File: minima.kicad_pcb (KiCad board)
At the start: 2 copper layers, 200.7 x 99.1 mm, 154 parts, among them J101 left_output, J102 left_input, J103 right_output, J104 right_input, J105 aux_power, J106 mains_voltage, J107 transformer_secondary, J108 transformer_primary, J109 earth, U201 LM1875, U202 LM1875, U301 NE5532, U302 NE5532, U303 NE5532, U304 NE5532, U401 LM7815_TO220, U402 LM7915_TO220

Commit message: The board shall now support single channel only.
Signed-off-by: Nenad Radulovic <nenad.radulovic@seavus.com>
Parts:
- removed C211, C218, C322, C324, C326, C328, C330, C332: 100n, Capacitor_SMD:C_1206_3216Metric_Pad1.24x1.80mm_HandSolder
- removed C212: 100u, Capacitor_THT:CP_Radial_D8.0mm_P3.50mm
- removed C213, C216, C219: 470u, Capacitor_THT:CP_Radial_D10.0mm_P5.00mm
- removed C214, C215, C220: 15p, Capacitor_SMD:C_0805_2012Metric_Pad1.15x1.50mm_HandSolder
- removed C217: 220n, Capacitor_SMD:C_1206_3216Metric_Pad1.24x1.80mm_HandSolder
- removed C321, C323, C325, C327, C329, C331: 10u, Capacitor_THT:CP_Radial_D5.0mm_P2.00mm
- removed C406, C408: 470n, Capacitor_THT:C_Rect_L9.0mm_W3.6mm_P7.50mm_MKT
- removed C407: 10n, Capacitor_THT:C_Rect_L9.0mm_W3.4mm_P7.50mm_MKT
- removed C409, C410: 10m, Capacitor_THT:CP_Radial_D35.0mm_P10.00mm_SnapIn
- removed D204: 1N5404, Diode_THT:D_DO-201AD_P12.70mm_Horizontal
- removed D303, D304: BAT54S, Package_TO_SOT_SMD:SOT-23_Handsoldering
- removed D401, D402: 1N4007, Diode_THT:D_DO-41_SOD81_P10.16mm_Horizontal
- removed D403: GBU1510, Diode_THT:Diode_Bridge_Vishay_GBU
- removed J105: aux_power, Connector_Phoenix_MC:PhoenixContact_MCV_1,5_4-G-3.5_1x04_P3.50mm_Vertical
- removed J106: mains_voltage, Connector_Phoenix_MC:PhoenixContact_MCV_1,5_2-G-3.81_1x02_P3.81mm_Vertical
- removed J107: transformer_secondary, Connector_Phoenix_MC:PhoenixContact_MCV_1,5_3-G-3.5_1x03_P3.50mm_Vertical
- removed J108: transformer_primary, Connector_Phoenix_MC:PhoenixContact_MCV_1,5_2-G-3.81_1x02_P3.81mm_Vertical
- removed J109: earth, Connector_Phoenix_MC:PhoenixContact_MCV_1,5_2-G-5.08_1x02_P5.08mm_Vertical
- removed L202: 2u, Choke_Axial_ThroughHole:Choke_Horizontal_RM15mm
- removed MH1, MH2: Mounting hole, MountingHole:MountingHole_3.2mm_M3_ISO14580_Pad
- removed MH3, MH4: Mounting Hole, MountingHole:MountingHole_3.2mm_M3_ISO14580_Pad
- removed R212, R219, R220, R224, R225: 3k9, Resistor_SMD:R_1206_3216Metric
- removed R213, R214, R226: 1k6, Resistor_SMD:R_1206_3216Metric
- removed R215, R221: 4.7, Resistor_THT:R_Axial_DIN0411_L9.9mm_D3.6mm_P15.24mm_Horizontal
- removed R216: 10, Resistor_THT:R_Axial_DIN0411_L9.9mm_D3.6mm_P15.24mm_Horizontal
- removed R217, R218, R222, R223: 270, Resistor_SMD:R_1206_3216Metric
- removed R321, R322, R323, R324: 100, Resistor_SMD:R_1206_3216Metric
- removed R405: 1, Resistor_THT:R_Axial_DIN0309_L9.0mm_D3.2mm_P12.70mm_Horizontal
- removed R406: 5k1, Resistor_THT:R_Axial_DIN0411_L9.9mm_D3.6mm_P12.70mm_Horizontal
- removed U202: LM1875, TO_SOT_Packages_THT:TO-220-5_Pentawatt_Multiwatt-5_Vertical_StaggeredType1
- removed U303, U304: NE5532, Housings_DIP:DIP-8_W7.62mm_LongPads
- removed U401: LM7815_TO220, TO_SOT_Packages_THT:TO-220_Vertical
- removed U402: LM7915_TO220, TO_SOT_Packages_THT:TO-220_Vertical
- added K201: FINDER-40.51, Relays_THT:Relay_SPDT_Finder_40.51, F.Cu at (182.6, 98.7)
- added LOGO1: KiCad Logo, Symbol:KiCad-Logo2_12mm_SilkScreen, F.Cu at (58.6, 118.7)
- added LOGO2: OSHW Logo, Symbol:OSHW-Logo2_14.6x12mm_SilkScreen, F.Cu at (210.6, 94.7)
- added MK101: Mounting_Hole, MountingHole:MountingHole_3.2mm_M3_ISO7380, F.Cu at (101.6, 51.7)
- added MK102: Mounting_Hole, MountingHole:MountingHole_3.2mm_M3_ISO7380, F.Cu at (101.6, 139.7)
- added MK103: Mounting_Hole, MountingHole:MountingHole_3.2mm_M3_ISO7380, F.Cu at (189.6, 139.7)
- added MK104: Mounting_Hole, MountingHole:MountingHole_3.2mm_M3_ISO7380, F.Cu at (189.6, 51.7)
- added Q401: PN2222A, Package_TO_SOT_THT:TO-92_Inline_Narrow_Oval, F.Cu at (187.6, 107.7)
- C202: value 100n -> 470u; footprint Capacitor_SMD:C_1206_3216Metric_Pad1.24x1.80mm_HandSolder -> Capacitor_THT:CP_Radial_D8.0mm_P3.50mm; moved to F.Cu
- C203: value 100u -> 220n; footprint Capacitor_THT:CP_Radial_D8.0mm_P3.50mm -> Capacitor_SMD:C_1206_3216Metric_Pad1.24x1.80mm_HandSolder; moved to B.Cu
- C204: moved to F.Cu
- C205: value 100u -> 100n; footprint Capacitor_THT:CP_Radial_D8.0mm_P3.50mm -> Capacitor_SMD:C_1206_3216Metric_Pad1.24x1.80mm_HandSolder
- C206: value 470u -> 100u; footprint Capacitor_THT:CP_Radial_D10.0mm_P5.00mm -> Capacitor_THT:CP_Radial_D8.0mm_P3.50mm
- C207: value 220n -> 470u; footprint Capacitor_SMD:C_1206_3216Metric_Pad1.24x1.80mm_HandSolder -> Capacitor_THT:CP_Radial_D8.0mm_P3.50mm; moved to F.Cu
- C209: value 100n -> 100u; footprint Capacitor_SMD:C_1206_3216Metric_Pad1.24x1.80mm_HandSolder -> Capacitor_THT:CP_Radial_D8.0mm_P3.50mm; moved to F.Cu
- C210: value 100u -> 15p; footprint Capacitor_THT:CP_Radial_D8.0mm_P3.50mm -> Capacitor_SMD:C_0805_2012Metric_Pad1.15x1.50mm_HandSolder; moved to B.Cu
- C301: value 10u -> 22p; footprint Capacitor_THT:CP_Radial_D5.0mm_P2.00mm -> Capacitor_SMD:C_0805_2012Metric_Pad1.15x1.50mm_HandSolder
- C302, C315, C317: value 10u -> 22u
- C303: value 10u -> 220p; footprint Capacitor_THT:CP_Radial_D5.0mm_P2.00mm -> Capacitor_SMD:C_0805_2012Metric_Pad1.15x1.50mm_HandSolder; moved to B.Cu
- C304: value 10u -> 1n; footprint Capacitor_THT:CP_Radial_D5.0mm_P2.00mm -> Capacitor_SMD:C_0805_2012Metric_Pad1.15x1.50mm_HandSolder; moved to B.Cu
- C305: value 220p -> 22p
- C306: value 1n -> 22p
- C307, C308, D301, D302: moved to B.Cu
- C309: value 220p -> 22u; footprint Capacitor_SMD:C_0805_2012Metric_Pad1.15x1.50mm_HandSolder -> Capacitor_THT:CP_Radial_D5.0mm_P2.00mm
- C310, C312: value 1n -> 22u; footprint Capacitor_SMD:C_0805_2012Metric_Pad1.15x1.50mm_HandSolder -> Capacitor_THT:CP_Radial_D5.0mm_P2.00mm
- C311: value 220p -> 100n; footprint Capacitor_SMD:C_0805_2012Metric_Pad1.15x1.50mm_HandSolder -> Capacitor_SMD:C_1206_3216Metric_Pad1.24x1.80mm_HandSolder
- C313, C314, C316, C319: value 10u -> 100n; footprint Capacitor_THT:CP_Radial_D5.0mm_P2.00mm -> Capacitor_SMD:C_1206_3216Metric_Pad1.24x1.80mm_HandSolder
- C320: value 100n -> 22p; footprint Capacitor_SMD:C_1206_3216Metric_Pad1.24x1.80mm_HandSolder -> Capacitor_SMD:C_0805_2012Metric_Pad1.15x1.50mm_HandSolder
- C401, C403: value 1m -> 4m7; footprint Capacitor_THT:CP_Radial_D12.5mm_P5.00mm -> Capacitor_THT:CP_Radial_D25.0mm_P10.00mm_SnapIn
- C402, C404: value 10u -> 1m; footprint Capacitor_THT:CP_Radial_D5.0mm_P2.00mm -> Capacitor_THT:CP_Radial_D12.5mm_P5.00mm
- C405: value 10n -> 100n; footprint Capacitor_THT:C_Rect_L13.0mm_W4.0mm_P10.00mm_FKS3_FKP3_MKS4 -> Capacitor_SMD:C_1206_3216Metric_Pad1.24x1.80mm_HandSolder
- D203: value 1N5404 -> 1N4148; footprint Diode_THT:D_DO-201AD_P12.70mm_Horizontal -> Diodes_THT:D_DO-35_SOD27_P7.62mm_Horizontal
- J101: value left_output -> output
- J102: value left_input -> input; footprint Connector_PinHeader_2.54mm:PinHeader_1x04_P2.54mm_Vertical -> TerminalBlock_Phoenix:TerminalBlock_Phoenix_MPT-0,5-4-2.54_1x04_P2.54mm_Horizontal
- J103: value right_output -> powersupply; footprint Connector_Phoenix_MC:PhoenixContact_MCV_1,5_2-G-3.5_1x02_P3.50mm_Vertical -> Connector_Phoenix_MC:PhoenixContact_MCV_1,5_6-G-3.5_1x06_P3.50mm_Vertical
- J104: value right_input -> ps_ctrl; footprint Connector_PinHeader_2.54mm:PinHeader_1x04_P2.54mm_Vertical -> Connector_IDC:IDC-Header_2x05_P2.54mm_Vertical
- R201: footprint Resistor_SMD:R_1206_3216Metric -> Resistor_SMD:R_1206_3216Metric_Pad1.24x1.80mm_HandSolder
- R202: value 4.7 -> 15k; footprint Resistor_THT:R_Axial_DIN0411_L9.9mm_D3.6mm_P15.24mm_Horizontal -> Resistor_SMD:R_1206_3216Metric_Pad1.24x1.80mm_HandSolder; moved to B.Cu
- R203: value 10 -> 4.7
- R204: value 270 -> 10; footprint Resistor_SMD:R_1206_3216Metric -> Resistor_THT:R_Axial_DIN0411_L9.9mm_D3.6mm_P15.24mm_Horizontal; moved to F.Cu
- R205: value 270 -> 499; footprint Resistor_SMD:R_1206_3216Metric -> Resistor_SMD:R_1206_3216Metric_Pad1.24x1.80mm_HandSolder
- R206: value 3k9 -> 15k; footprint Resistor_SMD:R_1206_3216Metric -> Resistor_SMD:R_1206_3216Metric_Pad1.24x1.80mm_HandSolder
- R207: value 3k9 -> 4.7; footprint Resistor_SMD:R_1206_3216Metric -> Resistor_THT:R_Axial_DIN0411_L9.9mm_D3.6mm_P15.24mm_Horizontal; moved to F.Cu
- R208: value 4.7 -> 499; footprint Resistor_THT:R_Axial_DIN0411_L9.9mm_D3.6mm_P15.24mm_Horizontal -> Resistor_SMD:R_1206_3216Metric_Pad1.24x1.80mm_HandSolder; moved to B.Cu
- R209, R210: value 270 -> 15k; footprint Resistor_SMD:R_1206_3216Metric -> Resistor_SMD:R_1206_3216Metric_Pad1.24x1.80mm_HandSolder
- R211: value 3k9 -> 1k6; footprint Resistor_SMD:R_1206_3216Metric -> Resistor_SMD:R_1206_3216Metric_Pad1.24x1.80mm_HandSolder
- R301, R304, R317, R318: value 10 -> 2k; footprint Resistor_SMD:R_1206_3216Metric -> Resistor_SMD:R_1206_3216Metric_Pad1.24x1.80mm_HandSolder
- R302, R303: value 10 -> 100; footprint Resistor_SMD:R_1206_3216Metric -> Resistor_SMD:R_1206_3216Metric_Pad1.24x1.80mm_HandSolder; moved to B.Cu
- R305: value 100 -> 49.9; footprint Resistor_SMD:R_1206_3216Metric -> Resistor_SMD:R_1206_3216Metric_Pad1.24x1.80mm_HandSolder
- R306: value 100 -> 2k; footprint Resistor_SMD:R_1206_3216Metric -> Resistor_SMD:R_1206_3216Metric_Pad1.24x1.80mm_HandSolder
- R307: value 100 -> 100k; footprint Resistor_SMD:R_1206_3216Metric -> Resistor_SMD:R_1206_3216Metric_Pad1.24x1.80mm_HandSolder; moved to B.Cu
- R308: value 100 -> 11k; footprint Resistor_SMD:R_1206_3216Metric -> Resistor_SMD:R_1206_3216Metric_Pad1.24x1.80mm_HandSolder; moved to B.Cu
- R309, R313: value 100k -> 2k; footprint Resistor_SMD:R_1206_3216Metric -> Resistor_SMD:R_1206_3216Metric_Pad1.24x1.80mm_HandSolder
- R310: value 10k -> 2k; footprint Resistor_SMD:R_1206_3216Metric -> Resistor_SMD:R_1206_3216Metric_Pad1.24x1.80mm_HandSolder
- R311: footprint Resistor_SMD:R_1206_3216Metric -> Resistor_SMD:R_1206_3216Metric_Pad1.24x1.80mm_HandSolder; moved to B.Cu
- R312: value 10k -> 11k; footprint Resistor_SMD:R_1206_3216Metric -> Resistor_SMD:R_1206_3216Metric_Pad1.24x1.80mm_HandSolder; moved to B.Cu
- R314: value 10k -> 49.9; footprint Resistor_SMD:R_1206_3216Metric -> Resistor_SMD:R_1206_3216Metric_Pad1.24x1.80mm_HandSolder
- R315: value 100k -> 100; footprint Resistor_SMD:R_1206_3216Metric -> Resistor_SMD:R_1206_3216Metric_Pad1.24x1.80mm_HandSolder; moved to B.Cu
- R316: value 10k -> 100; footprint Resistor_SMD:R_1206_3216Metric -> Resistor_SMD:R_1206_3216Metric_Pad1.24x1.80mm_HandSolder; moved to B.Cu
- R319, R320: value 10 -> 49.9; footprint Resistor_SMD:R_1206_3216Metric -> Resistor_SMD:R_1206_3216Metric_Pad1.24x1.80mm_HandSolder
- R401, R402: value 47 -> 1
- R403: value 1 -> 10; footprint Resistor_THT:R_Axial_DIN0309_L9.0mm_D3.2mm_P12.70mm_Horizontal -> Resistor_THT:R_Axial_DIN0411_L9.9mm_D3.6mm_P12.70mm_Horizontal
- R404: value 5k1 -> 1k; footprint Resistor_THT:R_Axial_DIN0411_L9.9mm_D3.6mm_P12.70mm_Horizontal -> Resistor_SMD:R_1206_3216Metric_Pad1.24x1.80mm_HandSolder; moved to B.Cu
- moved R303 378.1 mm to (109.6, 128.7)
- moved C309 378.1 mm to (117.6, 121.7), turned to 270 degrees
- moved R304 372.4 mm to (100.6, 88.2)
- moved R308 367.8 mm to (109.6, 119.2)
- moved C310 367.7 mm to (116.6, 78.7)
- moved R316 365.2 mm to (117.6, 128.7), turned to 180 degrees
- moved R312 364.6 mm to (117.6, 119.2)
- moved R302 363.5 mm to (108.1, 132.7), turned to 270 degrees
- moved R306 362.1 mm to (100.6, 92.7)
- moved R307 361.5 mm to (109.6, 126.2)
- moved C312 357.4 mm to (115.6, 60.7), turned to 180 degrees
- moved D302 356.5 mm to (123.1, 132.7), turned to 180 degrees
- moved C302 354.4 mm to (109.6, 121.7), turned to 270 degrees
- moved C308 351.9 mm to (115.6, 131.7)
- moved C315 348.2 mm to (110.6, 96.7), turned to 180 degrees
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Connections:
- C201 pad 1: Net-(C201-Pad1) -> /Input section/sgnd
- C202 pad 1: VCC -> Net-(C202-Pad1)
- C202 pad 2: GNDPWR -> /Power amplifier/inp
- C203 pad 1: VCC -> Net-(C203-Pad1)
- C203 pad 2: GNDPWR -> Net-(C203-Pad2)
- C204 pad 1: VCC -> Net-(C204-Pad1)
- C204 pad 2: GNDPWR -> /Power amplifier/spkhot
- C206 pad 1: Net-(C206-Pad1) -> VCC
- C206 pad 2: /Power amplifier/left_inp -> GNDPWR
- C207 pad 2: Net-(C207-Pad2) -> /Power amplifier/inn
- C208 pad 1: Net-(C208-Pad1) -> GNDPWR
- C208 pad 2: /Power amplifier/left_spkhot -> VEE
- C210 pad 1: GNDPWR -> Net-(C203-Pad2)
- C210 pad 2: VEE -> Net-(C210-Pad2)
- C301 pad 2: Net-(C301-Pad2) -> /Input section/sgnd
- C303 pad 1: Net-(C301-Pad1) -> Net-(C303-Pad1)
- C303 pad 2: Net-(C301-Pad2) -> /Input section/sgnd
- C304 pad 1: Net-(C302-Pad1) -> Net-(C302-Pad2)
- C304 pad 2: Net-(C302-Pad2) -> /Input section/sgnd
- C305 pad 2: GNDPWR -> Net-(C305-Pad2)
- C306 pad 1: Net-(C301-Pad2) -> Net-(C306-Pad1)
- C306 pad 2: GNDPWR -> /Input section/sgnd
- C307 pad 1: Net-(C307-Pad1) -> /Input section/sgnd
- C307 pad 2: GNDPWR -> Net-(C307-Pad2)
- C308 pad 1: Net-(C302-Pad2) -> /Input section/sgnd
- C308 pad 2: GNDPWR -> Net-(C308-Pad2)
- C309 pad 1: GNDPWR -> Net-(C309-Pad1)
- C309 pad 2: Net-(C309-Pad2) -> Net-(C308-Pad2)
- C310 pad 1: GNDPWR -> VDDA
- C310 pad 2: Net-(C310-Pad2) -> GNDPWR
- C311 pad 1: GNDPWR -> VDDA
- C311 pad 2: Net-(C311-Pad2) -> GNDPWR
- C312 pad 1: GNDPWR -> VDDA
- C312 pad 2: Net-(C312-Pad2) -> GNDPWR
- C313 pad 1: Net-(C313-Pad1) -> VDDA
- C313 pad 2: Net-(C310-Pad2) -> GNDPWR
- C314 pad 1: Net-(C314-Pad1) -> VDDA
- C314 pad 2: Net-(C312-Pad2) -> GNDPWR
- C315 pad 1: Net-(C313-Pad1) -> GNDPWR
- C315 pad 2: Net-(C310-Pad2) -> VSSA
- C316 pad 1: Net-(C314-Pad1) -> GNDPWR
- C316 pad 2: Net-(C312-Pad2) -> VSSA
- C317 pad 1: VDDA -> GNDPWR
- C317 pad 2: GNDPWR -> VSSA
- C318 pad 1: VDDA -> GNDPWR
- C318 pad 2: GNDPWR -> VSSA
- C319 pad 1: VDDA -> GNDPWR
- C319 pad 2: GNDPWR -> VSSA
- C320 pad 1: VDDA -> Net-(C320-Pad1)
- C320 pad 2: GNDPWR -> Net-(C320-Pad2)
- C401 pad 1: Net-(C401-Pad1) -> VCC
- C403 pad 2: Net-(C403-Pad2) -> VEE
- C405 pad 1: /Power supply/m2 -> GNDPWR
- C405 pad 2: /Power supply/m1 -> /Input section/sgnd
- D201 pad 2: /Power amplifier/left_spkhot -> /Power amplifier/spkhot
- D202 pad 1: /Power amplifier/left_spkhot -> /Power amplifier/spkhot
- D203 pad 1: VCC -> /Power amplifier/mutep
- D203 pad 2: /Power amplifier/right_spkhot -> /Power amplifier/muten
- D301 pad 3: Net-(C305-Pad1) -> Net-(C303-Pad1)
- D302 pad 3: Net-(C307-Pad1) -> Net-(C307-Pad2)
- J101 pad 1: /Power amplifier/left_spkhot -> /Power amplifier/spkhot
- J102 pad 1: /Input section/left_inp -> /Input section/inp
- J102 pad 2: GNDPWR -> /Input section/sgnd
- J102 pad 3: /Input section/left_inn -> /Input section/inn
- J102 pad 4: GNDPWR -> /Input section/sgnd
- J103 pad 1: /Power amplifier/right_spkhot -> /Power supply/ps_prevcc
- J103 pad 2: GNDPWR -> /Power supply/ps_prevee
- J104 pad 1: /Input section/right_inp -> /Power amplifier/mutep
- J104 pad 2: GNDPWR -> /Power supply/ps_ctrl_gnd
- J104 pad 3: /Input section/right_inn -> /Power supply/ps_ctrl_gnd
- J104 pad 4: GNDPWR -> /Power supply/ps_ctrl_op
- L201 pad 1: Net-(C207-Pad2) -> Net-(C203-Pad2)
- L201 pad 2: /Power amplifier/left_spkhot -> /Power amplifier/outp
- R201 pad 1: Net-(C201-Pad1) -> Net-(R201-Pad1)
- R201 pad 2: GNDPWR -> Net-(C201-Pad2)
- R202 pad 1: GNDPWR -> /Input section/sgnd
- R202 pad 2: Net-(C207-Pad1) -> Net-(R201-Pad1)
- R203 pad 2: Net-(C208-Pad1) -> Net-(C203-Pad1)
- R204 pad 1: Net-(R204-Pad1) -> GNDPWR
- R204 pad 2: Net-(C206-Pad1) -> Net-(C204-Pad1)
- R205 pad 1: Net-(C201-Pad2) -> Net-(R201-Pad1)
- R205 pad 2: Net-(R204-Pad1) -> Net-(C202-Pad1)
- R206 pad 1: Net-(R206-Pad1) -> /Input section/sgnd
- R206 pad 2: Net-(C201-Pad2) -> Net-(R201-Pad1)
- R207 pad 1: GNDPWR -> /Power amplifier/outp
- R207 pad 2: Net-(R206-Pad1) -> Net-(C203-Pad2)
- R208 pad 1: /Power amplifier/left_spkhot -> Net-(R208-Pad1)
- R208 pad 2: Net-(C207-Pad2) -> Net-(C207-Pad1)
- R209 pad 1: Net-(R209-Pad1) -> Net-(C203-Pad2)
- R209 pad 2: Net-(C213-Pad1) -> Net-(R208-Pad1)
- R210 pad 1: Net-(C214-Pad2) -> Net-(C203-Pad2)
- R210 pad 2: Net-(R209-Pad1) -> Net-(R208-Pad1)
- R211 pad 1: Net-(R211-Pad1) -> Net-(R208-Pad1)
- R211 pad 2: Net-(C214-Pad2) -> Net-(C210-Pad2)
- R301 pad 1: /Power amplifier/left_inp -> /Input section/sgnd
- R301 pad 2: Net-(R301-Pad2) -> Net-(C301-Pad1)
- R302 pad 1: /Power amplifier/left_inp -> Net-(C303-Pad1)
- R302 pad 2: Net-(R302-Pad2) -> /Input section/inp
- R303 pad 1: /Power amplifier/right_inp -> Net-(C302-Pad2)
- R303 pad 2: Net-(R303-Pad2) -> Net-(C303-Pad1)
- R304 pad 1: /Power amplifier/right_inp -> Net-(C301-Pad1)
- R305 pad 1: Net-(C305-Pad1) -> /Power amplifier/inp
- R305 pad 2: /Input section/left_inp -> Net-(C305-Pad2)
- R306 pad 1: Net-(C301-Pad2) -> Net-(C305-Pad1)
- R306 pad 2: Net-(C305-Pad1) -> Net-(R306-Pad2)
- R307 pad 1: Net-(C307-Pad1) -> Net-(C302-Pad2)
- R307 pad 2: /Input section/right_inp -> /Input section/sgnd
- R308 pad 1: Net-(C302-Pad2) -> Net-(C302-Pad1)
- R308 pad 2: Net-(C307-Pad1) -> /Input section/sgnd
- R309 pad 1: Net-(C301-Pad2) -> Net-(C305-Pad2)
- R309 pad 2: GNDPWR -> Net-(C305-Pad1)
- R310 pad 1: Net-(C301-Pad1) -> /Input section/sgnd
- R310 pad 2: GNDPWR -> Net-(C306-Pad1)
- R311 pad 1: Net-(C302-Pad2) -> /Input section/sgnd
- R311 pad 2: GNDPWR -> Net-(C308-Pad2)
- R312 pad 1: Net-(C302-Pad1) -> /Input section/sgnd
- R312 pad 2: GNDPWR -> Net-(C309-Pad1)
- R313 pad 1: GNDPWR -> Net-(C306-Pad1)
- R313 pad 2: Net-(C310-Pad2) -> Net-(R304-Pad2)
- R314 pad 1: GNDPWR -> /Power amplifier/inp
- R314 pad 2: Net-(C313-Pad1) -> Net-(C320-Pad2)
- R315 pad 1: GNDPWR -> Net-(C307-Pad2)
- R315 pad 2: Net-(C312-Pad2) -> /Input section/inn
- R316 pad 1: GNDPWR -> Net-(C308-Pad2)
- R316 pad 2: Net-(C314-Pad1) -> Net-(C307-Pad2)
- R317 pad 1: /Power amplifier/left_inn -> Net-(C320-Pad1)
- R317 pad 2: Net-(R317-Pad2) -> Net-(R306-Pad2)
- R318 pad 1: /Power amplifier/left_inn -> Net-(C320-Pad2)
- R318 pad 2: Net-(R318-Pad2) -> Net-(C320-Pad1)
- R319 pad 1: /Power amplifier/right_inn -> /Power amplifier/inn
- R319 pad 2: Net-(R319-Pad2) -> /Input section/sgnd
- R320 pad 1: /Power amplifier/right_inn -> /Power amplifier/inn
- R320 pad 2: Net-(R320-Pad2) -> /Input section/sgnd
- R401 pad 1: Net-(C401-Pad1) -> VDDA
- R401 pad 2: VCC -> /Power supply/ps_prevcc
- R402 pad 1: Net-(C403-Pad2) -> VSSA
- R402 pad 2: VEE -> /Power supply/ps_prevee
- R403 pad 1: Net-(C406-Pad2) -> /Input section/sgnd
- R404 pad 1: VCC -> Net-(Q401-Pad2)
- R404 pad 2: GNDPWR -> /Power supply/ps_ctrl_op
- U201 pad 1: Net-(C201-Pad2) -> Net-(R201-Pad1)
- U201 pad 2: Net-(C214-Pad2) -> Net-(R208-Pad1)
- U201 pad 4: Net-(C207-Pad2) -> Net-(C203-Pad2)
- U301 pad 1: Net-(R301-Pad2) -> Net-(R304-Pad2)
- U301 pad 2: Net-(R301-Pad2) -> Net-(R304-Pad2)
- U301 pad 3: Net-(C301-Pad1) -> Net-(C302-Pad1)
- U301 pad 5: Net-(C301-Pad1) -> Net-(C309-Pad1)
- U301 pad 6: Net-(R302-Pad2) -> Net-(R306-Pad2)
- U301 pad 7: Net-(R302-Pad2) -> Net-(R306-Pad2)
- U302 pad 1: Net-(R303-Pad2) -> Net-(C305-Pad2)
- U302 pad 2: Net-(R303-Pad2) -> Net-(C305-Pad1)
- U302 pad 3: Net-(C302-Pad1) -> Net-(C301-Pad1)
- U302 pad 5: Net-(C302-Pad1) -> Net-(C306-Pad1)
- U302 pad 6: Net-(R304-Pad2) -> Net-(C320-Pad1)
- U302 pad 7: Net-(R304-Pad2) -> Net-(C320-Pad2)
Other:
- board size 200.7 x 99.1 mm -> 100 x 100 mm

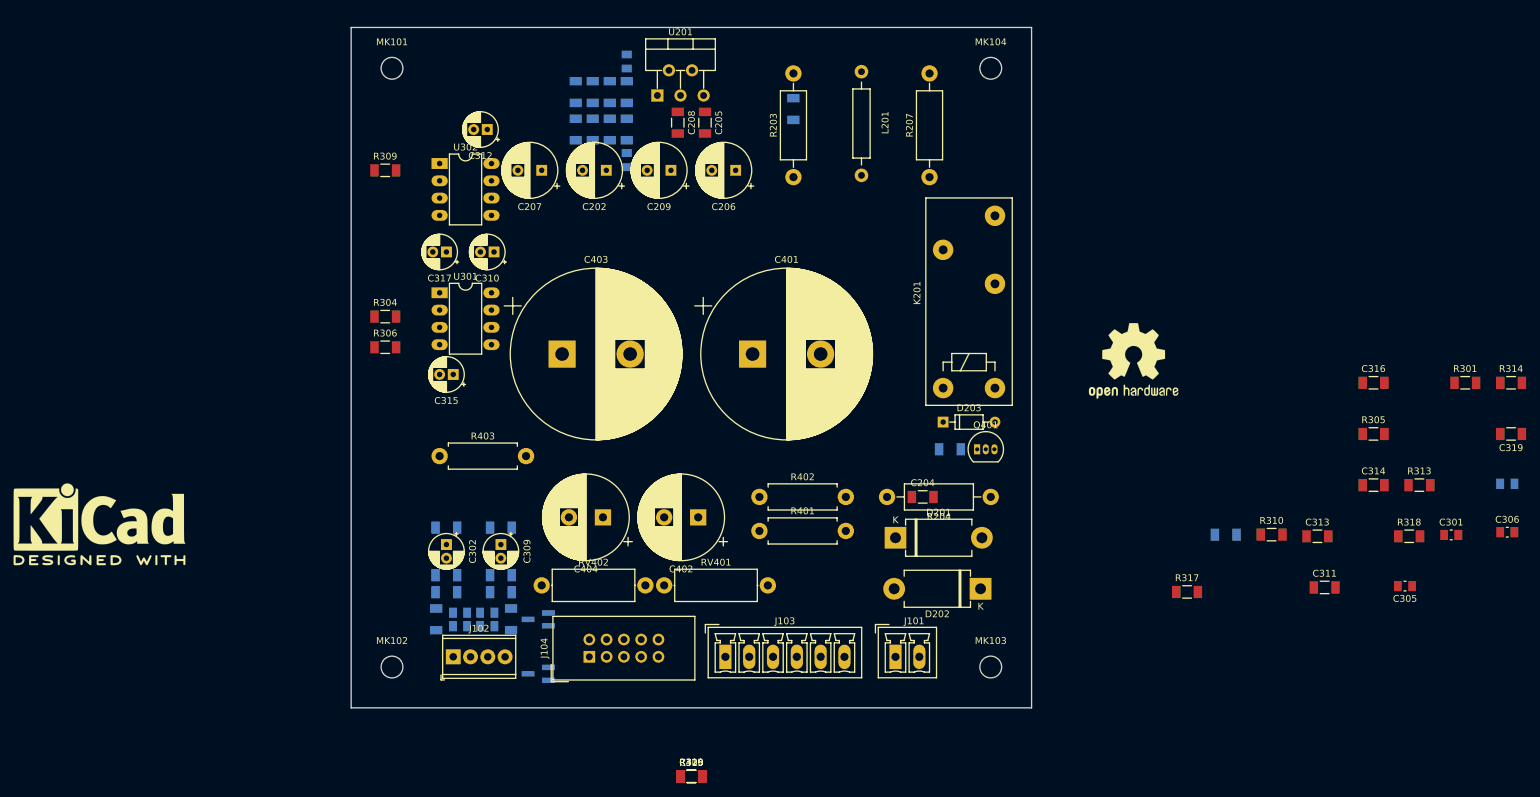
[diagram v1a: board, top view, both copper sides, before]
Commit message: Switched to Kicad 5.0
Signed-off-by: Nenad Radulovic <nenad.b.radulovic@gmail.com>
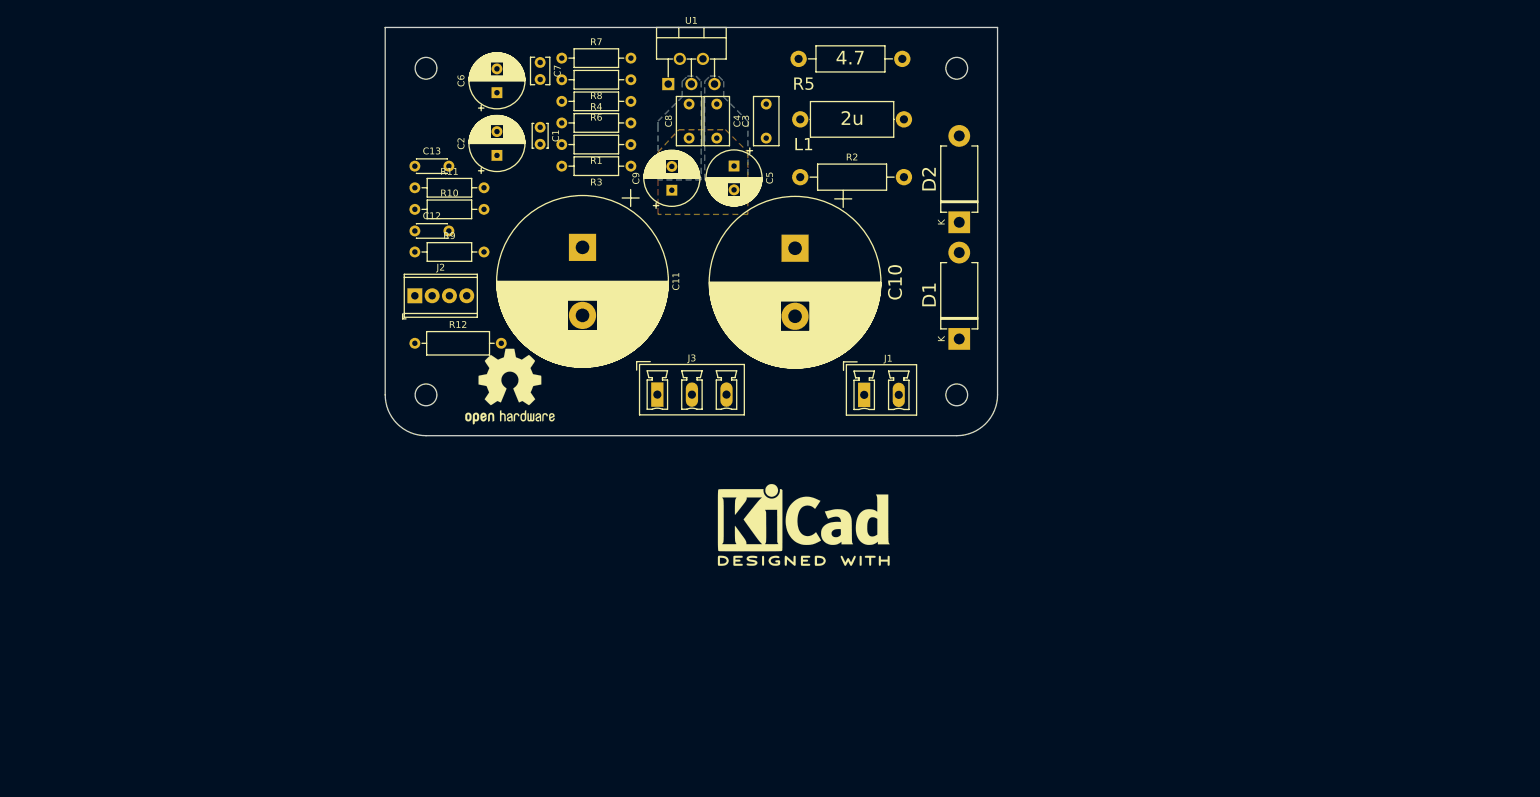
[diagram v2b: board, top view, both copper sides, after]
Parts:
- removed C201, C210: 15p, Capacitor_SMD:C_0805_2012Metric_Pad1.15x1.50mm_HandSolder
- removed C202, C207: 470u, Capacitor_THT:CP_Radial_D8.0mm_P3.50mm
- removed C203: 220n, Capacitor_SMD:C_1206_3216Metric_Pad1.24x1.80mm_HandSolder
- removed C204, C205, C208, C311, C313, C314, C316, C318, C319, C405: 100n, Capacitor_SMD:C_1206_3216Metric_Pad1.24x1.80mm_HandSolder
- removed C206, C209: 100u, Capacitor_THT:CP_Radial_D8.0mm_P3.50mm
- removed C301, C305, C306, C320: 22p, Capacitor_SMD:C_0805_2012Metric_Pad1.15x1.50mm_HandSolder
- removed C302, C309, C310, C312, C315, C317: 22u, Capacitor_THT:CP_Radial_D5.0mm_P2.00mm
- removed C303, C307: 220p, Capacitor_SMD:C_0805_2012Metric_Pad1.15x1.50mm_HandSolder
- removed C304, C308: 1n, Capacitor_SMD:C_0805_2012Metric_Pad1.15x1.50mm_HandSolder
- removed C401, C403: 4m7, Capacitor_THT:CP_Radial_D25.0mm_P10.00mm_SnapIn
- removed C402, C404: 1m, Capacitor_THT:CP_Radial_D12.5mm_P5.00mm
- removed D201, D202: 1N5404, Diode_THT:D_DO-201AD_P12.70mm_Horizontal
- removed D203: 1N4148, Diodes_THT:D_DO-35_SOD27_P7.62mm_Horizontal
- removed D301, D302: BAT54S, Package_TO_SOT_SMD:SOT-23_Handsoldering
- removed J101: output, Connector_Phoenix_MC:PhoenixContact_MCV_1,5_2-G-3.5_1x02_P3.50mm_Vertical
- removed J102: input, TerminalBlock_Phoenix:TerminalBlock_Phoenix_MPT-0,5-4-2.54_1x04_P2.54mm_Horizontal
- removed J103: powersupply, Connector_Phoenix_MC:PhoenixContact_MCV_1,5_6-G-3.5_1x06_P3.50mm_Vertical
- removed J104: ps_ctrl, Connector_IDC:IDC-Header_2x05_P2.54mm_Vertical
- removed K201: FINDER-40.51, Relays_THT:Relay_SPDT_Finder_40.51
- removed L201: 2u, Choke_Axial_ThroughHole:Choke_Horizontal_RM15mm
- removed MK101, MK102, MK103, MK104: Mounting_Hole, MountingHole:MountingHole_3.2mm_M3_ISO7380
- removed Q401: PN2222A, Package_TO_SOT_THT:TO-92_Inline_Narrow_Oval
- removed R201, R211: 1k6, Resistor_SMD:R_1206_3216Metric_Pad1.24x1.80mm_HandSolder
- removed R202, R206, R209, R210: 15k, Resistor_SMD:R_1206_3216Metric_Pad1.24x1.80mm_HandSolder
- removed R203, R207: 4.7, Resistor_THT:R_Axial_DIN0411_L9.9mm_D3.6mm_P15.24mm_Horizontal
- removed R204: 10, Resistor_THT:R_Axial_DIN0411_L9.9mm_D3.6mm_P15.24mm_Horizontal
- removed R205, R208: 499, Resistor_SMD:R_1206_3216Metric_Pad1.24x1.80mm_HandSolder
- removed R301, R304, R306, R309, R310, R313, R317, R318: 2k, Resistor_SMD:R_1206_3216Metric_Pad1.24x1.80mm_HandSolder
- removed R302, R303, R315, R316: 100, Resistor_SMD:R_1206_3216Metric_Pad1.24x1.80mm_HandSolder
- removed R305, R314, R319, R320: 49.9, Resistor_SMD:R_1206_3216Metric_Pad1.24x1.80mm_HandSolder
- removed R307, R311: 100k, Resistor_SMD:R_1206_3216Metric_Pad1.24x1.80mm_HandSolder
- removed R308, R312: 11k, Resistor_SMD:R_1206_3216Metric_Pad1.24x1.80mm_HandSolder
- removed R401, R402: 1, Resistor_THT:R_Axial_DIN0411_L9.9mm_D3.6mm_P12.70mm_Horizontal
- removed R403: 10, Resistor_THT:R_Axial_DIN0411_L9.9mm_D3.6mm_P12.70mm_Horizontal
- removed R404: 1k, Resistor_SMD:R_1206_3216Metric_Pad1.24x1.80mm_HandSolder
- removed RV401, RV402: Varistor, Resistor_THT:R_Axial_DIN0414_L11.9mm_D4.5mm_P15.24mm_Horizontal
- removed U201: LM1875, TO_SOT_Packages_THT:TO-220-5_Pentawatt_Multiwatt-5_Vertical_StaggeredType1
- removed U301, U302: NE5532, Housings_DIP:DIP-8_W7.62mm_LongPads
- added C1: 15p, Capacitor_THT:C_Disc_D3.4mm_W2.1mm_P2.50mm, F.Cu at (123.3, 60.4)
- added C10: 4m7, Capacitor_THT:CP_Radial_D25.0mm_P10.00mm_SnapIn, F.Cu at (160.8, 78.2)
- added C11: 4m7, Capacitor_THT:CP_Radial_D25.0mm_P10.00mm_SnapIn, F.Cu at (129.6, 78.0)
- added C12: 220p, Capacitor_THT:C_Disc_D4.3mm_W1.9mm_P5.00mm, F.Cu at (104.9, 75.6)
- added C13: 1n, Capacitor_THT:C_Disc_D4.3mm_W1.9mm_P5.00mm, F.Cu at (104.9, 66.1)
- added C2: 470u, Capacitor_THT:CP_Radial_D8.0mm_P3.50mm, F.Cu at (117.0, 64.5)
- added C3: 220n, Capacitor_THT:C_Rect_L7.0mm_W3.5mm_P5.00mm, F.Cu at (156.6, 62.0)
- added C4: 100n, Capacitor_THT:C_Rect_L7.0mm_W3.5mm_P5.00mm, F.Cu at (149.3, 57.0)
- added C5: 100u, Capacitor_THT:CP_Radial_D8.0mm_P3.50mm, F.Cu at (151.8, 66.1)
- added C6: 470u, Capacitor_THT:CP_Radial_D8.0mm_P3.50mm, F.Cu at (117.0, 55.3)
- added C7: 15p, Capacitor_THT:C_Disc_D3.8mm_W2.6mm_P2.50mm, F.Cu at (123.3, 50.9)
- added C8: 100n, Capacitor_THT:C_Rect_L7.0mm_W3.5mm_P5.00mm, F.Cu at (145.2, 62.0)
- added C9: 100u, Capacitor_THT:CP_Radial_D8.0mm_P3.50mm, F.Cu at (142.7, 69.6)
- added D1: 1N5404, Diode_THT:D_DO-201AD_P12.70mm_Horizontal, F.Cu at (184.9, 91.5)
- added D2: 1N5404, Diode_THT:D_DO-201AD_P12.70mm_Horizontal, F.Cu at (184.9, 74.4)
- added J1: output, Connector_Phoenix_MC_HighVoltage:PhoenixContact_MCV_1,5_2-G-5.08_1x02_P5.08mm_Vertical, F.Cu at (171.0, 99.7)
- added J2: input, TerminalBlock_Phoenix:TerminalBlock_Phoenix_MPT-0,5-4-2.54_1x04_P2.54mm_Horizontal, F.Cu at (104.9, 85.2)
- added J3: powersupply, Connector_Phoenix_MC_HighVoltage:PhoenixContact_MCV_1,5_3-G-5.08_1x03_P5.08mm_Vertical, F.Cu at (140.6, 99.7)
- added L1: 2u, Inductor_THT:L_Axial_L12.0mm_D5.0mm_P15.24mm_Horizontal_Fastron_MISC, F.Cu at (161.6, 59.2)
- added MK1: Mounting_Hole, MountingHole:MountingHole_3.2mm_M3_ISO7380, F.Cu at (106.6, 99.7)
- added MK2: Mounting_Hole, MountingHole:MountingHole_3.2mm_M3_ISO7380, F.Cu at (106.6, 51.7)
- added MK3: Mounting_Hole, MountingHole:MountingHole_3.2mm_M3_ISO7380, F.Cu at (184.6, 51.7)
- added MK4: Mounting_Hole, MountingHole:MountingHole_3.2mm_M3_ISO7380, F.Cu at (184.6, 99.7)
- added R1: 1k6, Resistor_THT:R_Axial_DIN0207_L6.3mm_D2.5mm_P10.16mm_Horizontal, F.Cu at (136.7, 62.9)
- added R10: 100, Resistor_THT:R_Axial_DIN0207_L6.3mm_D2.5mm_P10.16mm_Horizontal, F.Cu at (104.9, 72.5)
- added R11: 100k, Resistor_THT:R_Axial_DIN0207_L6.3mm_D2.5mm_P10.16mm_Horizontal, F.Cu at (104.9, 69.3)
- added R12: 10, Resistor_THT:R_Axial_DIN0309_L9.0mm_D3.2mm_P12.70mm_Horizontal, F.Cu at (104.9, 92.1)
- added R2: 4.7, Resistor_THT:R_Axial_DIN0411_L9.9mm_D3.6mm_P15.24mm_Horizontal, F.Cu at (161.6, 67.7)
- added R3: 499, Resistor_THT:R_Axial_DIN0207_L6.3mm_D2.5mm_P10.16mm_Horizontal, F.Cu at (136.7, 66.1)
- added R4: 15k, Resistor_THT:R_Axial_DIN0207_L6.3mm_D2.5mm_P10.16mm_Horizontal, F.Cu at (126.5, 59.8)
- added R5: 4.7, Resistor_THT:R_Axial_DIN0411_L9.9mm_D3.6mm_P15.24mm_Horizontal, F.Cu at (176.6, 50.3)
- added R6: 499, Resistor_THT:R_Axial_DIN0207_L6.3mm_D2.5mm_P10.16mm_Horizontal, F.Cu at (136.7, 56.6)
- added R7: 15k, Resistor_THT:R_Axial_DIN0207_L6.3mm_D2.5mm_P10.16mm_Horizontal, F.Cu at (126.5, 50.2)
- added R8: 1k6, Resistor_THT:R_Axial_DIN0207_L6.3mm_D2.5mm_P10.16mm_Horizontal, F.Cu at (136.7, 53.4)
- added R9: 100, Resistor_THT:R_Axial_DIN0207_L6.3mm_D2.5mm_P10.16mm_Horizontal, F.Cu at (104.9, 78.7)
- added U1: LM1875, Package_TO_SOT_THT:TO-220-5_P3.4x3.7mm_StaggerOdd_Lead3.8mm_Vertical, F.Cu at (142.2, 54.0)
- moved LOGO1 103.5 mm to (162.1, 118.8)
- moved LOGO2 91.7 mm to (118.9, 98.5)
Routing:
- added copper zone on F.Cu, net GNDPWR
- added copper zone on B.Cu, net VCC
- added copper zone on B.Cu, net VEE
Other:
- board size 100 x 100 mm -> 90 x 60 mm

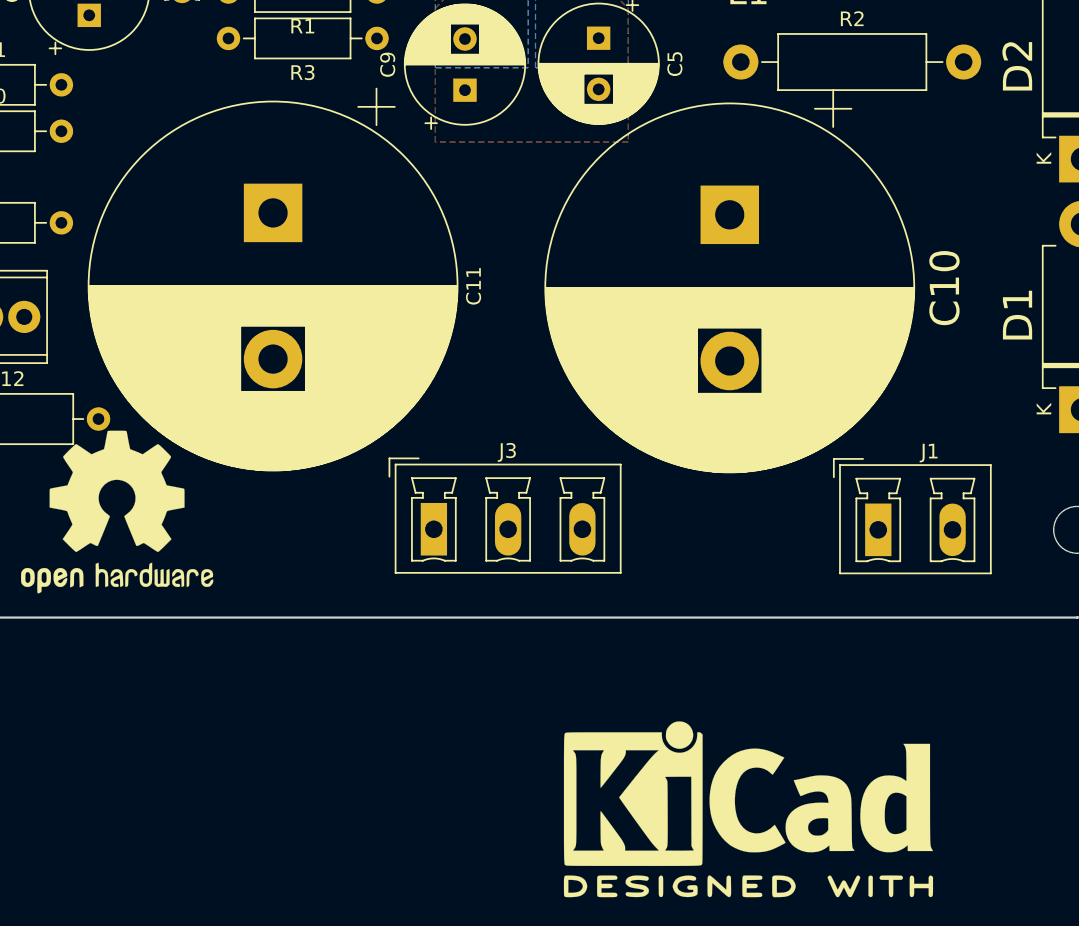
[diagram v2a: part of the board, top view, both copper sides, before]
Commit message: Updated regarding v5.0
Still updateing regarding transition to v5.0
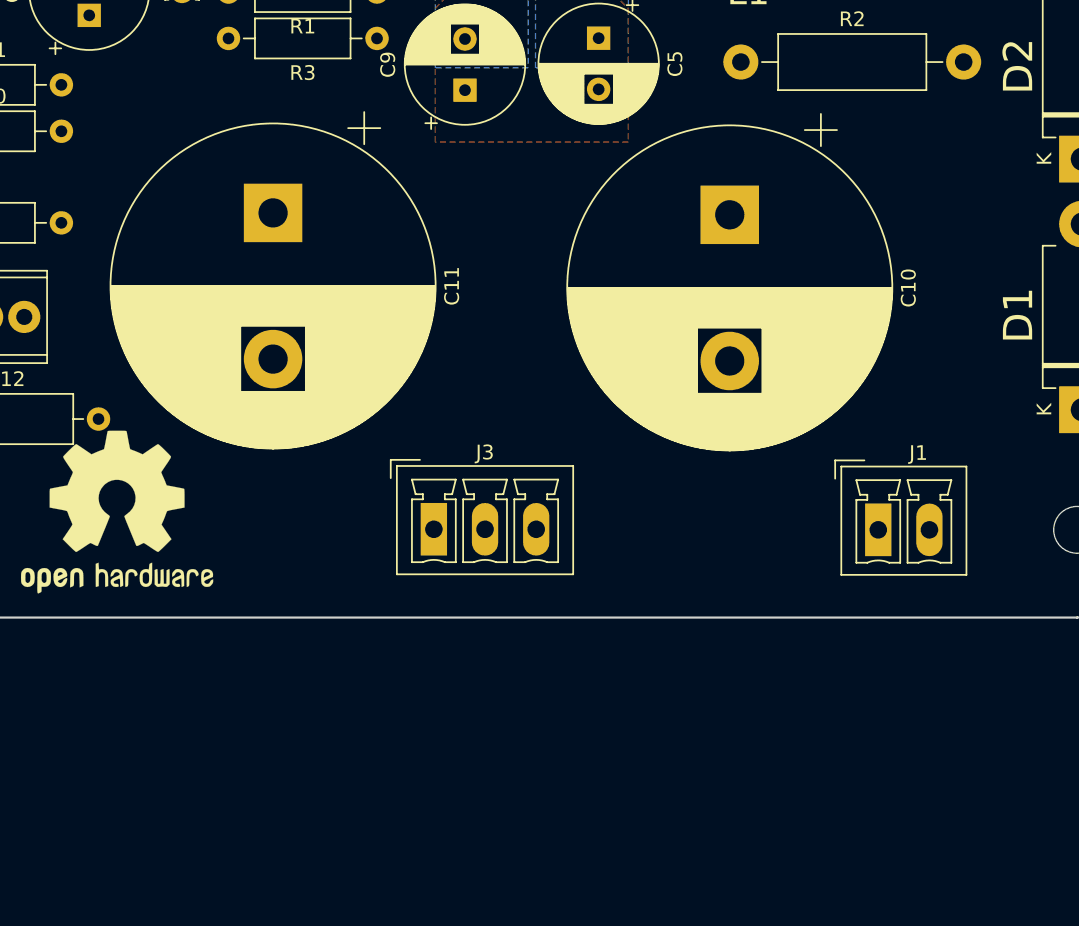
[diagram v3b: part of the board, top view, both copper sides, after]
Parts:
- removed LOGO1: KiCad Logo, Symbol:KiCad-Logo2_12mm_SilkScreen
- C10, C11: footprint Capacitor_THT:CP_Radial_D25.0mm_P10.00mm_SnapIn -> Capacitor_THT:CP_Radial_D22.0mm_P10.00mm_SnapIn
- J1: footprint Connector_Phoenix_MC_HighVoltage:PhoenixContact_MCV_1,5_2-G-5.08_1x02_P5.08mm_Vertical -> Connector_Phoenix_MC:PhoenixContact_MCV_1,5_2-G-3.5_1x02_P3.50mm_Vertical
- J3: footprint Connector_Phoenix_MC_HighVoltage:PhoenixContact_MCV_1,5_3-G-5.08_1x03_P5.08mm_Vertical -> Connector_Phoenix_MC:PhoenixContact_MCV_1,5_3-G-3.5_1x03_P3.50mm_Vertical
